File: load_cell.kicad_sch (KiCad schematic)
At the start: 1 part, among them J11 4-Pin Load Cell

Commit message: do some pcb routing
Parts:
- renumbered J11 to J3
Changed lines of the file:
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@@
 		(dnp no)
 		(fields_autoplaced yes)
-		(property "Reference" "#PWR0115"
+		(property "Reference" "#PWR025"
 			(at 138.43 111.76 0)
 			(hide yes)
@@
 			(project "gse_control_node"
 				(path "/24817451-dfe0-4b9a-9d93-7304529c9d58/3fe78498-f3da-4a4e-905d-c6815bbc6a4f"
-					(reference "#PWR0115")
+					(reference "#PWR025")
 					(unit 1)
 				)
@@
 		(dnp no)
 		(fields_autoplaced yes)
-		(property "Reference" "#PWR01"
+		(property "Reference" "#PWR024"
 			(at 138.43 99.06 0)
 			(hide yes)
@@
 			(project "gse_control_node"
 				(path "/24817451-dfe0-4b9a-9d93-7304529c9d58/3fe78498-f3da-4a4e-905d-c6815bbc6a4f"
-					(reference "#PWR01")
+					(reference "#PWR024")
 					(unit 1)
 				)
@@
 		(dnp no)
 		(fields_autoplaced yes)
-		(property "Reference" "J11"
+		(property "Reference" "J3"
 			(at 147.32 99.0599 0)
 			(show_name no)
@@
 			(project "gse_control_node"
 				(path "/24817451-dfe0-4b9a-9d93-7304529c9d58/3fe78498-f3da-4a4e-905d-c6815bbc6a4f"
-					(reference "J11")
+					(reference "J3")
 					(unit 1)
 				)

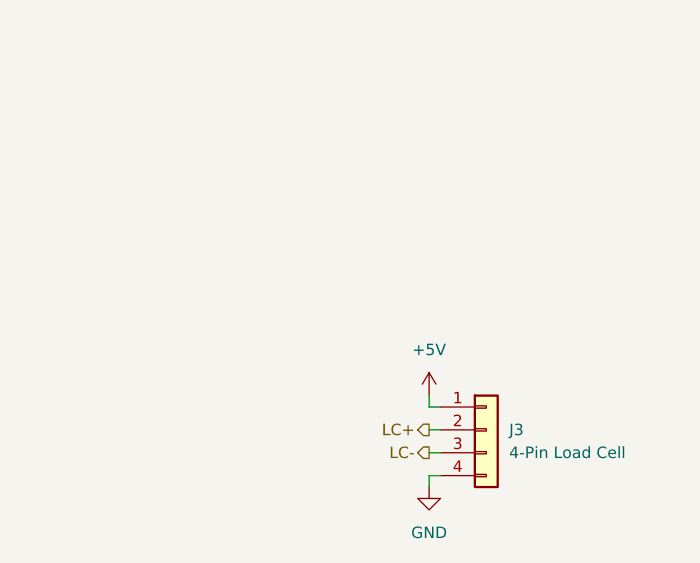
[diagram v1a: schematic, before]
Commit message: remove unneccesary component fields
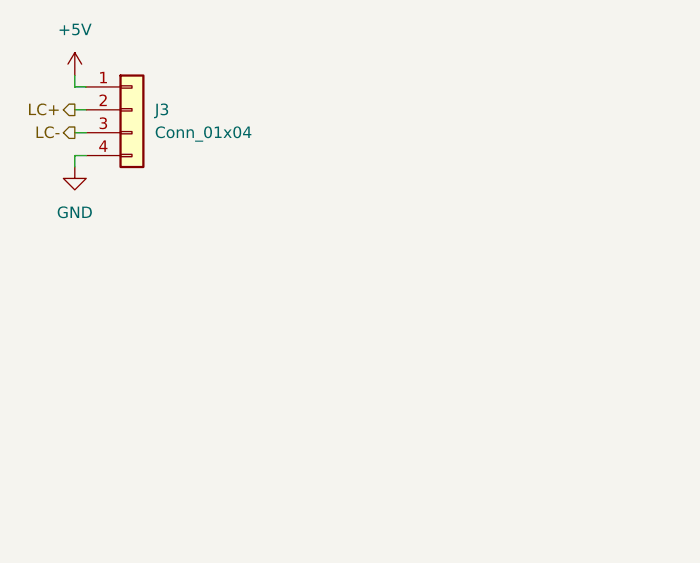
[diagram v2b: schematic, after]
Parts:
- J3: value 4-Pin Load Cell -> Conn_01x04; LCSC (none) -> N/A
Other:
- moved on the sheet: J3
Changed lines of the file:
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@@
 	(generator "eeschema")
 	(generator_version "10.0")
-	(paper "A4")
-	(wire
-		(pts
-			(xy 138.43 101.6) (xy 139.7 101.6)
-		)
-		(stroke
-			(width 0)
-			(type default)
-		)
-	)
-	(wire
-		(pts
-			(xy 138.43 95.25) (xy 138.43 96.52)
-		)
-		(stroke
-			(width 0)
-			(type default)
-		)
-	)
-	(wire
-		(pts
-			(xy 138.43 105.41) (xy 138.43 104.14)
-		)
-		(stroke
-			(width 0)
-			(type default)
-		)
-	)
-	(wire
-		(pts
-			(xy 138.43 99.06) (xy 139.7 99.06)
-		)
-		(stroke
-			(width 0)
-			(type default)
-		)
-	)
-	(wire
-		(pts
-			(xy 138.43 96.52) (xy 139.7 96.52)
-		)
-		(stroke
-			(width 0)
-			(type default)
-		)
-	)
-	(wire
-		(pts
-			(xy 138.43 104.14) (xy 139.7 104.14)
+	(paper "A5")
+	(wire
+		(pts
+			(xy 99.06 66.04) (xy 100.33 66.04)
+		)
+		(stroke
+			(width 0)
+			(type default)
+		)
+	)
+	(wire
+		(pts
+			(xy 99.06 59.69) (xy 99.06 60.96)
+		)
+		(stroke
+			(width 0)
+			(type default)
+		)
+	)
+	(wire
+		(pts
+			(xy 99.06 69.85) (xy 99.06 68.58)
+		)
+		(stroke
+			(width 0)
+			(type default)
+		)
+	)
+	(wire
+		(pts
+			(xy 99.06 63.5) (xy 100.33 63.5)
+		)
+		(stroke
+			(width 0)
+			(type default)
+		)
+	)
+	(wire
+		(pts
+			(xy 99.06 60.96) (xy 100.33 60.96)
+		)
+		(stroke
+			(width 0)
+			(type default)
+		)
+	)
+	(wire
+		(pts
+			(xy 99.06 68.58) (xy 100.33 68.58)
 		)
 		(stroke
@@
 	(hierarchical_label "LC-"
 		(shape output)
-		(at 138.43 101.6 180)
+		(at 99.06 66.04 180)
 		(effects
 			(font
@@
 	(hierarchical_label "LC+"
 		(shape output)
-		(at 138.43 99.06 180)
+		(at 99.06 63.5 180)
 		(effects
 			(font
@@
 	(symbol
 		(lib_id "power:GND")
-		(at 138.43 105.41 0)
+		(at 99.06 69.85 0)
 		(unit 1)
 		(body_style 1)
@@
 		(fields_autoplaced yes)
 		(property "Reference" "#PWR025"
-			(at 138.43 111.76 0)
+			(at 99.06 76.2 0)
 			(hide yes)
 			(show_name no)
@@
 		)
 		(property "Value" "GND"
-			(at 138.43 110.49 0)
+			(at 99.06 74.93 0)
 			(show_name no)
 			(do_not_autoplace no)
@@
 		)
 		(property "Footprint" ""
-			(at 138.43 105.41 0)
+			(at 99.06 69.85 0)
 			(hide yes)
 			(show_name no)
@@
 		)
 		(property "Datasheet" ""
-			(at 138.43 105.41 0)
+			(at 99.06 69.85 0)
 			(hide yes)
 			(show_name no)
@@
 		)
 		(property "Description" "Power symbol creates a global label with name \"GND\" , ground"
-			(at 138.43 105.41 0)
+			(at 99.06 69.85 0)
 			(hide yes)
 			(show_name no)
@@
 	(symbol
 		(lib_id "power:+5V")
-		(at 138.43 95.25 0)
+		(at 99.06 59.69 0)
 		(unit 1)
 		(body_style 1)
@@
 		(fields_autoplaced yes)
 		(property "Reference" "#PWR024"
-			(at 138.43 99.06 0)
+			(at 99.06 63.5 0)
 			(hide yes)
 			(show_name no)
@@
 		)
 		(property "Value" "+5V"
-			(at 138.43 90.17 0)
+			(at 99.06 54.61 0)
 			(show_name no)
 			(do_not_autoplace no)
@@
 		)
 		(property "Footprint" ""
-			(at 138.43 95.25 0)
+			(at 99.06 59.69 0)
 			(hide yes)
 			(show_name no)
@@
 		)
 		(property "Datasheet" ""
-			(at 138.43 95.25 0)
+			(at 99.06 59.69 0)
 			(hide yes)
 			(show_name no)
@@
 		)
 		(property "Description" "Power symbol creates a global label with name \"+5V\""
-			(at 138.43 95.25 0)
+			(at 99.06 59.69 0)
 			(hide yes)
 			(show_name no)
@@
 	(symbol
 		(lib_id "Connector_Generic:Conn_01x04")
-		(at 144.78 99.06 0)
+		(at 105.41 63.5 0)
 		(unit 1)
 		(body_style 1)
@@
 		(in_bom no)
 		(on_board yes)
-		(in_pos_files yes)
+		(in_pos_files no)
 		(dnp no)
 		(fields_autoplaced yes)
 		(property "Reference" "J3"
-			(at 147.32 99.0599 0)
+			(at 107.95 63.4999 0)
 			(show_name no)
 			(do_not_autoplace no)
@@
 			)
 		)
-		(property "Value" "4-Pin Load Cell"
-			(at 147.32 101.5999 0)
+		(property "Value" "Conn_01x04"
+			(at 107.95 66.0399 0)
 			(show_name no)
 			(do_not_autoplace no)
@@
 		)
 		(property "Footprint" "Connector_Molex:Molex_Micro-Fit_3.0_43650-0415_1x04_P3.00mm_Vertical"
-			(at 144.78 99.06 0)
+			(at 105.41 63.5 0)
 			(hide yes)
 			(show_name no)
@@
 		)
 		(property "Datasheet" ""
-			(at 144.78 99.06 0)
+			(at 105.41 63.5 0)
 			(hide yes)
 			(show_name no)
@@
 		)
 		(property "Description" "Generic connector, single row, 01x04, script generated (kicad-library-utils/schlib/autogen/connector/)"
-			(at 144.78 99.06 0)
-			(hide yes)
-			(show_name no)
-			(do_not_autoplace no)
-			(effects
-				(font
-					(size 1.27 1.27)
-				)
-			)
-		)
-		(property "ADC Number" ""
-			(at 144.78 99.06 0)
-			(hide yes)
-			(show_name no)
-			(do_not_autoplace no)
-			(effects
-				(font
-					(size 1.27 1.27)
-				)
-			)
-		)
-		(property "DCR" ""
-			(at 144.78 99.06 0)
-			(hide yes)
-			(show_name no)
-			(do_not_autoplace no)
-			(effects
-				(font
-					(size 1.27 1.27)
-				)
-			)
-		)
-		(property "I2C Address" ""
-			(at 144.78 99.06 0)
-			(hide yes)
-			(show_name no)
-			(do_not_autoplace no)
-			(effects
-				(font
-					(size 1.27 1.27)
-				)
-			)
-		)
-		(property "Irated" ""
-			(at 144.78 99.06 0)
-			(hide yes)
-			(show_name no)
-			(do_not_autoplace no)
-			(effects
-				(font
-					(size 1.27 1.27)
-				)
-			)
-		)
-		(property "Isat" ""
-			(at 144.78 99.06 0)
-			(hide yes)
-			(show_name no)
-			(do_not_autoplace no)
-			(effects
-				(font
-					(size 1.27 1.27)
-				)
-			)
-		)
-		(property "MFG" ""
-			(at 144.78 99.06 0)
-			(hide yes)
-			(show_name no)
-			(do_not_autoplace no)
-			(effects
-				(font
-					(size 1.27 1.27)
-				)
-			)
-		)
-		(property "MFR" ""
-			(at 144.78 99.06 0)
-			(hide yes)
-			(show_name no)
+			(at 105.41 63.5 0)
+			(hide yes)
+			(show_name no)
+			(do_not_autoplace no)
+			(effects
+				(font
+					(size 1.27 1.27)
+				)
+			)
+		)
+		(property "LCSC" "N/A"
+			(at 105.41 63.5 0)
+			(hide yes)
+			(show_name no)

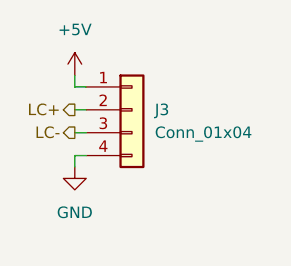
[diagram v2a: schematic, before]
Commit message: switch load cell connector to 5 pin with shield
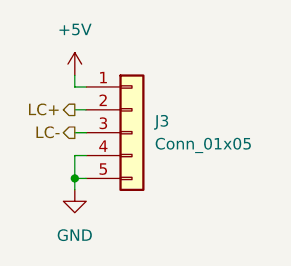
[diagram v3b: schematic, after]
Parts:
- J3: value Conn_01x04 -> Conn_01x05; footprint Connector_Molex:Molex_Micro-Fit_3.0_43650-0415_1x04_P3.00mm_Vertical -> Connector_Molex:Molex_Micro-Fit_3.0_43650-0515_1x05_P3.00mm_Vertical; symbol Connector_Generic:Conn_01x04 -> Connector_Generic:Conn_01x05; now in the parts list
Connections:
- net GND: now also J3.5 (Pin_5)
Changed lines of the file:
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@@
 	(generator_version "10.0")
 	(paper "A5")
+	(junction
+		(at 99.06 71.12)
+		(diameter 0)
+		(color 0 0 0 0)
+	)
+	(wire
+		(pts
+			(xy 99.06 71.12) (xy 99.06 68.58)
+		)
+		(stroke
+			(width 0)
+			(type default)
+		)
+	)
+	(wire
+		(pts
+			(xy 99.06 59.69) (xy 99.06 60.96)
+		)
+		(stroke
+			(width 0)
+			(type default)
+		)
+	)
 	(wire
 		(pts
@@
 	(wire
 		(pts
-			(xy 99.06 59.69) (xy 99.06 60.96)
-		)
-		(stroke
-			(width 0)
-			(type default)
-		)
-	)
-	(wire
-		(pts
-			(xy 99.06 69.85) (xy 99.06 68.58)
+			(xy 99.06 72.39) (xy 99.06 71.12)
+		)
+		(stroke
+			(width 0)
+			(type default)
+		)
+	)
+	(wire
+		(pts
+			(xy 99.06 68.58) (xy 100.33 68.58)
+		)
+		(stroke
+			(width 0)
+			(type default)
+		)
+	)
+	(wire
+		(pts
+			(xy 99.06 60.96) (xy 100.33 60.96)
 		)
 		(stroke
@@
 	(wire
 		(pts
-			(xy 99.06 60.96) (xy 100.33 60.96)
-		)
-		(stroke
-			(width 0)
-			(type default)
-		)
-	)
-	(wire
-		(pts
-			(xy 99.06 68.58) (xy 100.33 68.58)
+			(xy 99.06 71.12) (xy 100.33 71.12)
 		)
 		(stroke
@@
 	(symbol
 		(lib_id "power:GND")
-		(at 99.06 69.85 0)
+		(at 99.06 72.39 0)
 		(unit 1)
 		(body_style 1)
@@
 		(fields_autoplaced yes)
 		(property "Reference" "#PWR025"
-			(at 99.06 76.2 0)
+			(at 99.06 78.74 0)
 			(hide yes)
 			(show_name no)
@@
 		)
 		(property "Value" "GND"
-			(at 99.06 74.93 0)
+			(at 99.06 77.47 0)
 			(show_name no)
 			(do_not_autoplace no)
@@
 		)
 		(property "Footprint" ""
-			(at 99.06 69.85 0)
+			(at 99.06 72.39 0)
 			(hide yes)
 			(show_name no)
@@
 		)
 		(property "Datasheet" ""
-			(at 99.06 69.85 0)
+			(at 99.06 72.39 0)
 			(hide yes)
 			(show_name no)
@@
 		)
 		(property "Description" "Power symbol creates a global label with name \"GND\" , ground"
-			(at 99.06 69.85 0)
+			(at 99.06 72.39 0)
 			(hide yes)
 			(show_name no)
@@
 	)
 	(symbol
-		(lib_id "Connector_Generic:Conn_01x04")
-		(at 105.41 63.5 0)
+		(lib_id "Connector_Generic:Conn_01x05")
+		(at 105.41 66.04 0)
 		(unit 1)
 		(body_style 1)
 		(exclude_from_sim no)
-		(in_bom no)
+		(in_bom yes)
 		(on_board yes)
-		(in_pos_files no)
+		(in_pos_files yes)
 		(dnp no)
 		(fields_autoplaced yes)
 		(property "Reference" "J3"
-			(at 107.95 63.4999 0)
+			(at 107.95 64.7699 0)
 			(show_name no)
 			(do_not_autoplace no)
@@
 			)
 		)
-		(property "Value" "Conn_01x04"
-			(at 107.95 66.0399 0)
+		(property "Value" "Conn_01x05"
+			(at 107.95 67.3099 0)
 			(show_name no)
 			(do_not_autoplace no)
@@
 			)
 		)
-		(property "Footprint" "Connector_Molex:Molex_Micro-Fit_3.0_43650-0415_1x04_P3.00mm_Vertical"
-			(at 105.41 63.5 0)
+		(property "Footprint" "Connector_Molex:Molex_Micro-Fit_3.0_43650-0515_1x05_P3.00mm_Vertical"
+			(at 105.41 66.04 0)
 			(hide yes)
 			(show_name no)
@@
 		)
 		(property "Datasheet" ""
-			(at 105.41 63.5 0)
-			(hide yes)
-			(show_name no)
-			(do_not_autoplace no)
-			(effects
-				(font
-					(size 1.27 1.27)
-				)
-			)
-		)
-		(property "Description" "Generic connector, single row, 01x04, script generated (kicad-library-utils/schlib/autogen/connector/)"
-			(at 105.41 63.5 0)
+			(at 105.41 66.04 0)
+			(hide yes)
+			(show_name no)
+			(do_not_autoplace no)
+			(effects
+				(font
+					(size 1.27 1.27)
+				)
+			)
+		)
+		(property "Description" "Generic connector, single row, 01x05, script generated (kicad-library-utils/schlib/autogen/connector/)"
+			(at 105.41 66.04 0)
 			(hide yes)
 			(show_name no)
@@
 		)
 		(property "LCSC" "N/A"
-			(at 105.41 63.5 0)
+			(at 105.41 66.04 0)
 			(hide yes)
 			(show_name no)
@@
 		(pin "3"
 		)
+		(pin "5"
+		)
 		(instances

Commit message: fix load cell silkscreen
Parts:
- J3: now left out of the parts list
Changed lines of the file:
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@@
 		(body_style 1)
 		(exclude_from_sim no)
-		(in_bom yes)
+		(in_bom no)
 		(on_board yes)
-		(in_pos_files yes)
+		(in_pos_files no)
 		(dnp no)
 		(fields_autoplaced yes)
